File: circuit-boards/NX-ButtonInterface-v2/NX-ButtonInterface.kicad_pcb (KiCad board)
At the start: 2 copper layers, 58.4 x 22.5 mm, 2 parts, among them J1 NX CONTROL & UART, J2 NX BUTTON

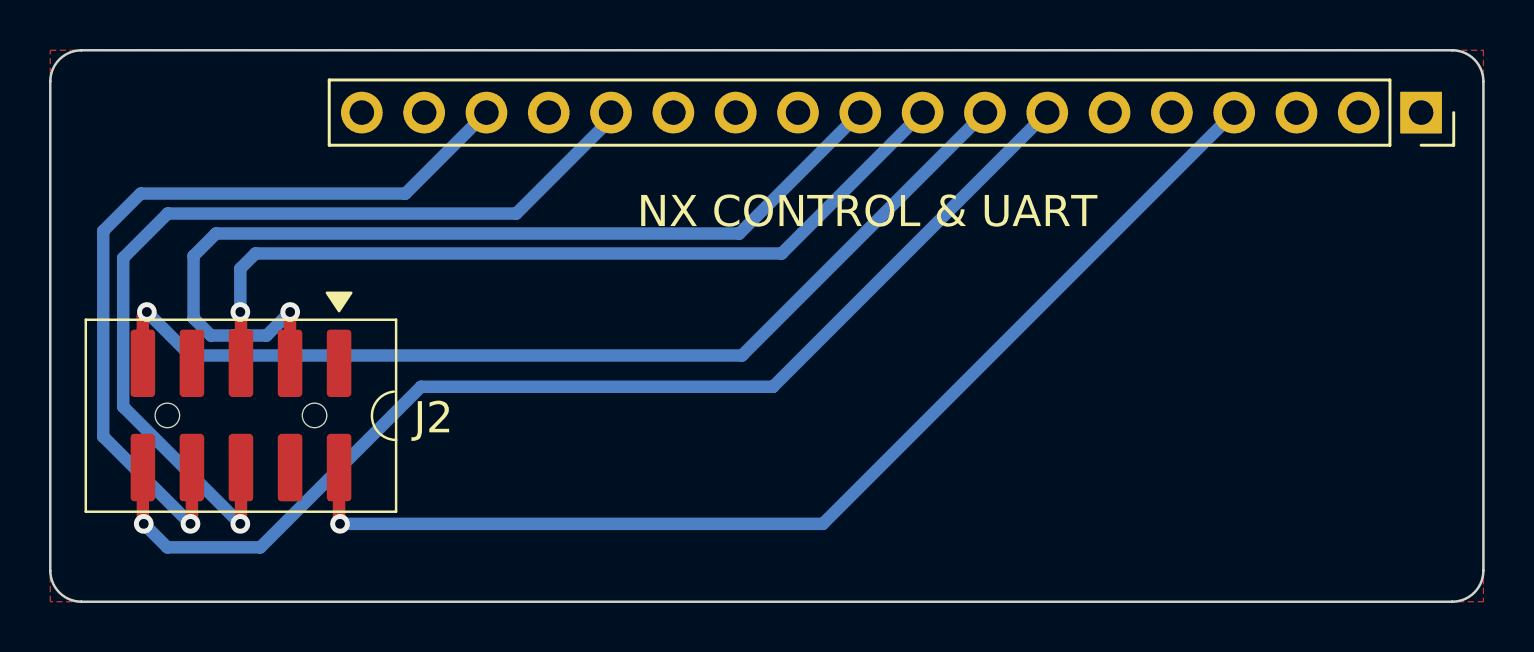
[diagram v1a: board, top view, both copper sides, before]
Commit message: adjust header to match nx-adapter
Signed-off-by: Scott Berman <sgberman1@gmail.com>
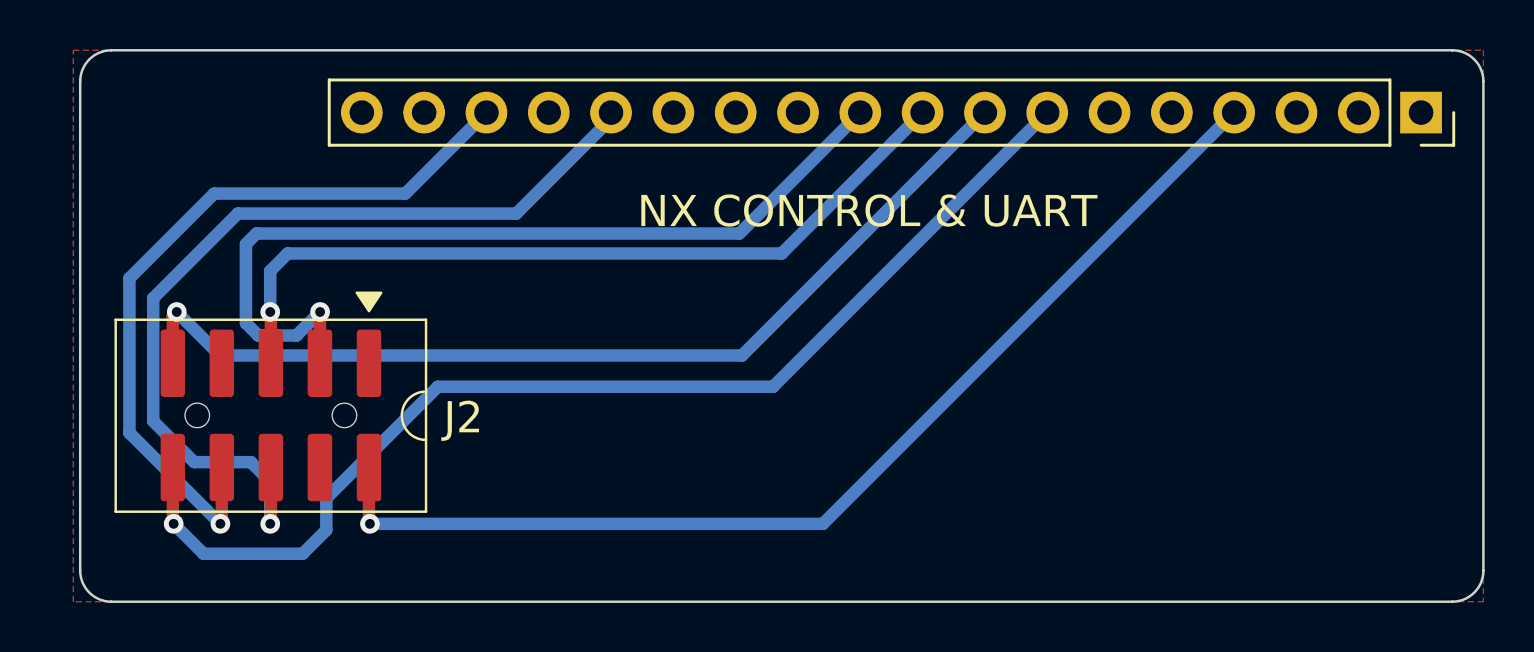
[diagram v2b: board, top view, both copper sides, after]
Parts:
- added LOGO1: SPACE COOKIES LOGO, NX-ButtonInterface:SPACE_COOKIES_LOGO_15mm, B.Cu at (122.5, 102.7)
- moved J2 1.22 mm to (83.0, 105.3)
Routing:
- net /UART2_TXD: track 38.9 -> 36.2 mm
- net /~{REC}: track 33.3 -> 31.2 mm
- net /UART2_RXD: track 34.3 -> 33.0 mm
- net /NX_PC_LED+: track 41.2 -> 39.9 mm
- net /3V3: track 45.7 -> 44.5 mm
- net /~{SYS_RESET}: track 37.6 -> 36.8 mm
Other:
- board size 58.4 x 22.5 mm -> 57.2 x 22.5 mm
- board text added: "1868 SPACE COOKIES"
- board text added: "NX BUTTON INTERFACE V2 2025"
- board text removed: "2025 NX BUTTON INTERFACE V2"

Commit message: Update NX-ButtonInterface-v2 to be compatible with NX-J401-Adapter-v5
Signed-off-by: Scott Berman <sgberman1@gmail.com>
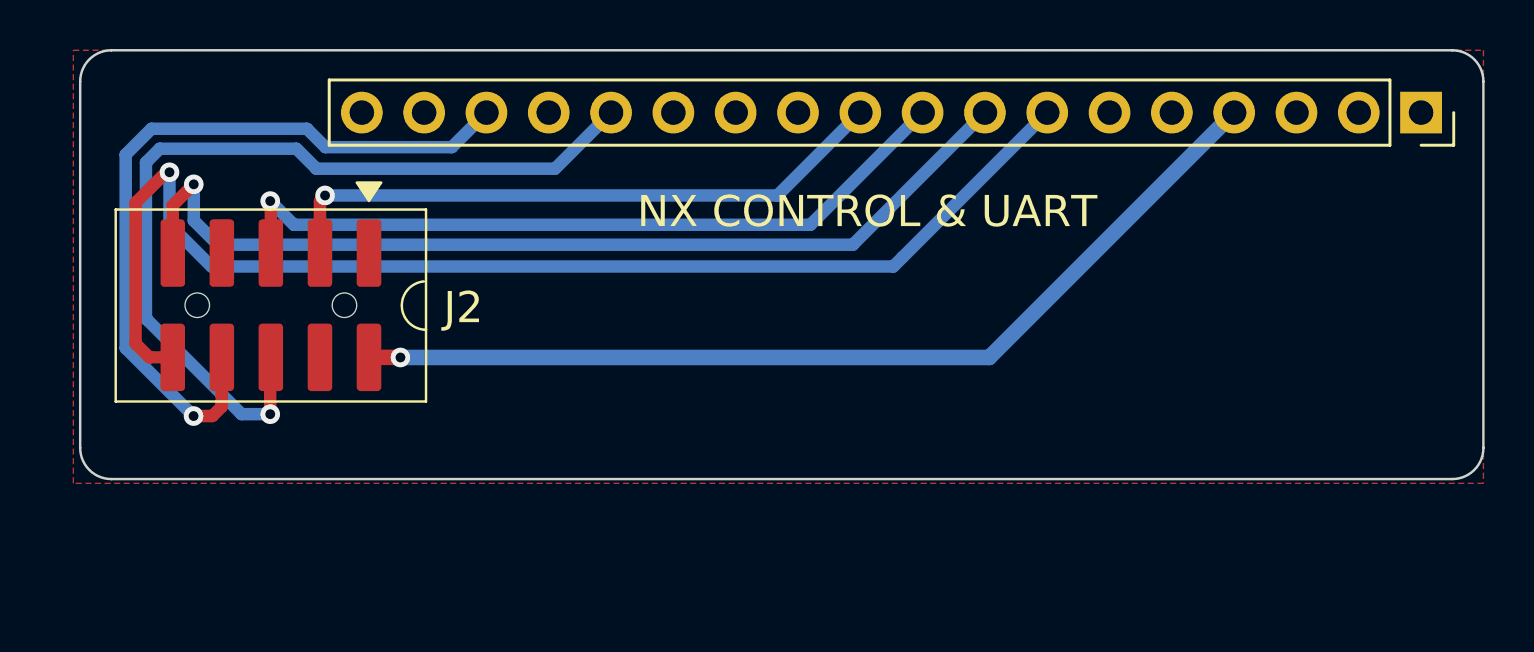
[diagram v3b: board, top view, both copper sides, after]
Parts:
- moved J2 4.49 mm to (83.0, 100.8)
- moved LOGO1 1.97 mm to (123.2, 100.8)
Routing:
- net /UART2_TXD: track 36.2 -> 25.7 mm
- net /3V3: track 44.5 -> 39.4 mm
- net /NX_PC_LED-: track 46.6 -> 50.6 mm
- net /UART2_RXD: track 33.0 -> 31.0 mm
- net /~{SYS_RESET}: track 36.8 -> 36.1 mm
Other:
- board size 57.2 x 22.5 mm -> 57.2 x 17.5 mm
- board text added: "2252.00 mils x 688.15 mils"
- board text removed: "1900.00 mils x 835.00 mils"
- board text removed: "BACK"
